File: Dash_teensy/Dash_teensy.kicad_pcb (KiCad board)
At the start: 2 copper layers, 72 parts, among them J1 J1B1211CCD, J10 2060-452_998-404, J11 2060-452_998-404, J12 J1B1211CCD, J13 BM04B-GHS-TBT_LF__SN_, J14 BM04B-GHS-TBT_LF__SN_, J15 2060-452_998-404, J2 2060-452_998-404, J3 2060-452_998-404, J4 2060-452_998-404, J5 2060-452_998-404, J6 2060-452_998-404, J7 2060-452_998-404, J8 J1B1211CCD, J9 2060-452_998-404, U1 DEV-16771, U10 MCP2562FDT-E/SN, U11 MCP2562FDT-E/SN, U12 MCP2562FDT-E/SN, U2 DEV-16771, U3 DEV-16771, U4 MCP2562FDT-E/SN, U5 MCP2562FDT-E/SN, U6 MCP2562FDT-E/SN, U7 MCP2562FDT-E/SN, U8 MCP2562FDT-E/SN, U9 MCP2562FDT-E/SN

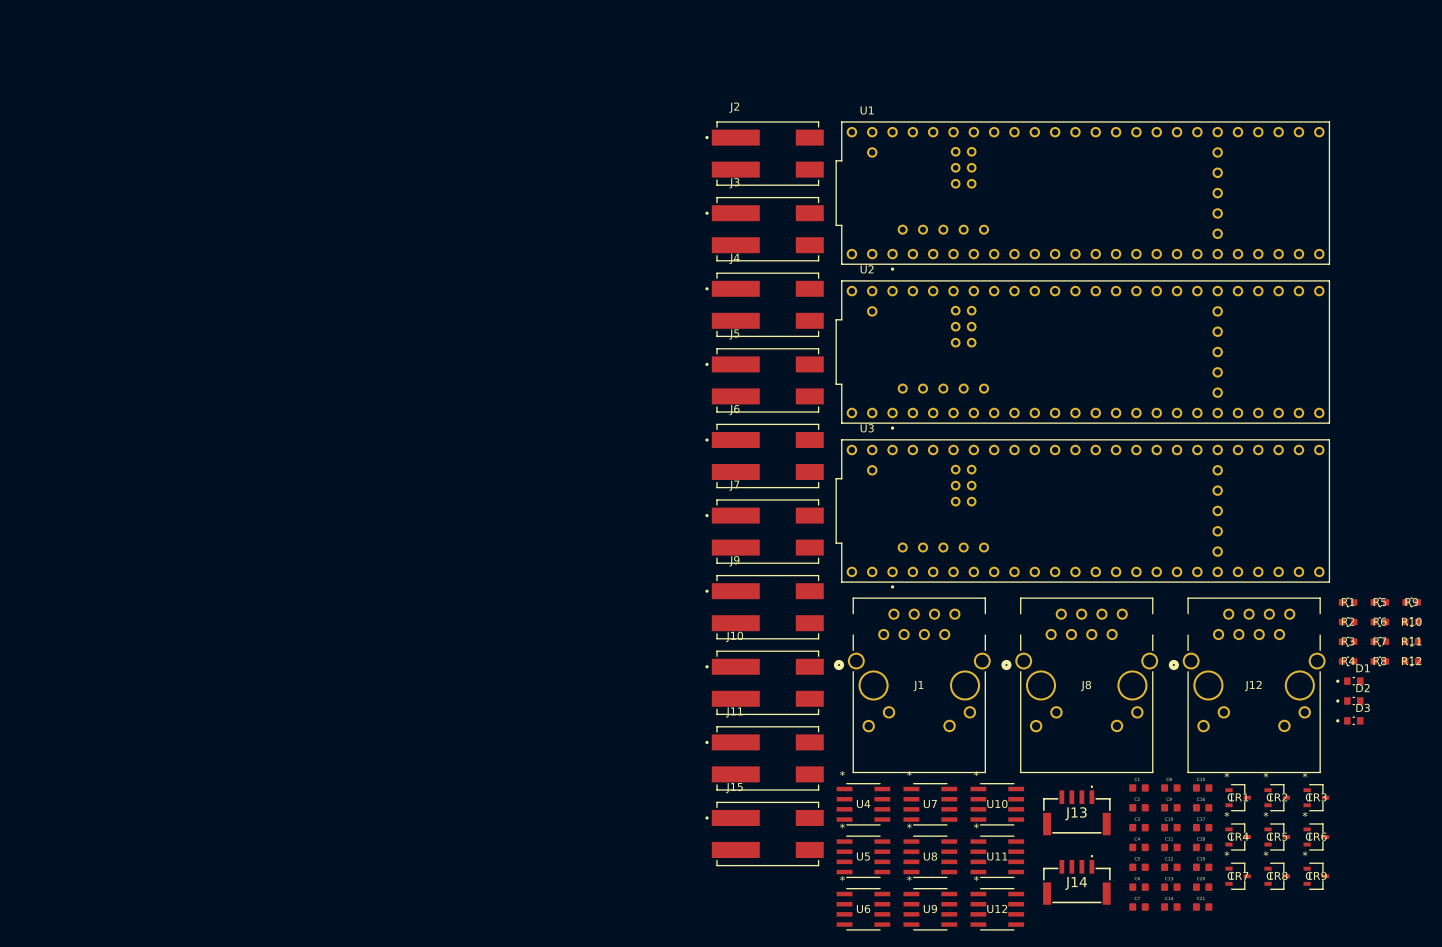
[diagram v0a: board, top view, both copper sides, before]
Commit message: figured out placement
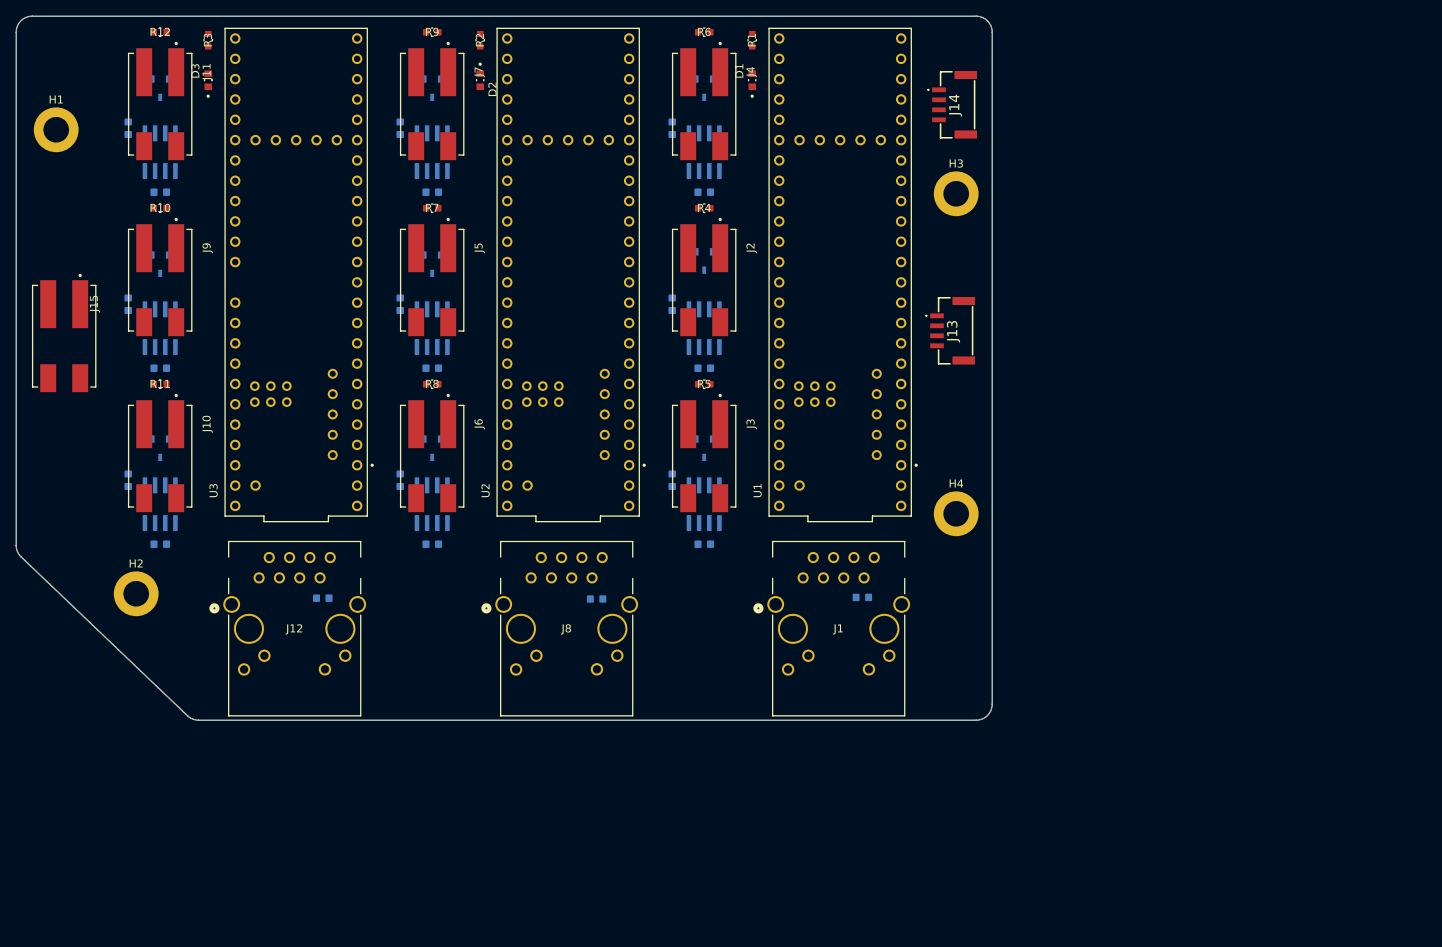
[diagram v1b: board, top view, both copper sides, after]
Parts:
- added H1: MountingHole, MountingHole:MountingHole_3.2mm_M3_DIN965_Pad, F.Cu at (40.0, 64.2)
- added H2: MountingHole, MountingHole:MountingHole_3.2mm_M3_DIN965_Pad, F.Cu at (50.0, 122.2)
- added H3: MountingHole, MountingHole:MountingHole_3.2mm_M3_DIN965_Pad, F.Cu at (152.5, 72.2)
- added H4: MountingHole, MountingHole:MountingHole_3.2mm_M3_DIN965_Pad, F.Cu at (152.5, 112.2)
- C1, C10, C11, C12, C13, C14, C15, C16, C17, C18, C19, C2, C20, C21, C3, C4, C5, C6, C7, C8, C9, CR1, CR2, CR3, CR4, CR5, CR6, CR7, CR8, CR9, U10, U11, U12, U4, U5, U6, U7, U8, U9: moved to B.Cu
- moved R12 175.1 mm to (53.0, 52.0)
- moved CR9 174.9 mm to (53.0, 59.0), turned to -90 degrees
- moved R10 164.8 mm to (53.0, 74.0)
- moved D3 164.1 mm to (59.0, 58.0), turned to 90 degrees
- moved C18 161.6 mm to (49.0, 64.0), turned to 90 degrees
- moved R3 161.1 mm to (59.0, 53.0), turned to 90 degrees
- moved R11 159.7 mm to (53.0, 96.0)
- moved CR7 154.9 mm to (53.0, 81.0), turned to -90 degrees
- moved C15 150.1 mm to (53.0, 72.0)
- moved CR8 149.5 mm to (53.0, 104.0), turned to -90 degrees
- moved C16 148.3 mm to (49.0, 86.0), turned to 90 degrees
- moved CR6 144.8 mm to (87.0, 59.0), turned to -90 degrees
- moved C13 142.0 mm to (53.0, 94.0)
- moved R9 141.7 mm to (87.0, 52.0)
- moved C17 141.2 mm to (49.0, 108.0), turned to 90 degrees
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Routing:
- net /ET1+: track 0.00 -> 0.59 mm
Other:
- board outline added: 122 x 88 mm
